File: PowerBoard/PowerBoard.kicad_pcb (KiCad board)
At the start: 2 copper layers, 95 x 72 mm, 26 parts, among them J1 AC_IN, J2 RelayCoil, J3 GATE_DRIVE, J4 LOGIC, J5 DC_LINK, K1 ALQ305

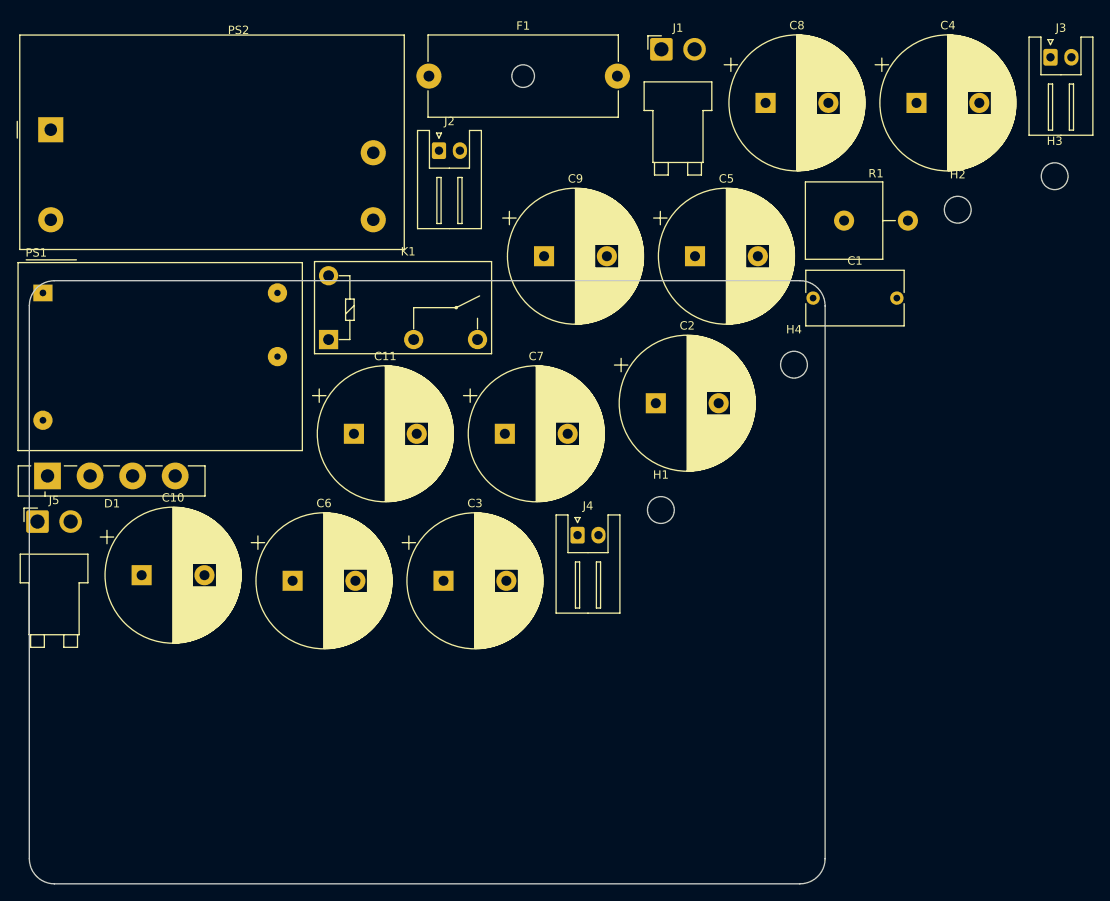
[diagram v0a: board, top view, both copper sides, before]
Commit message: コンデンサを一つ減らして配線完了
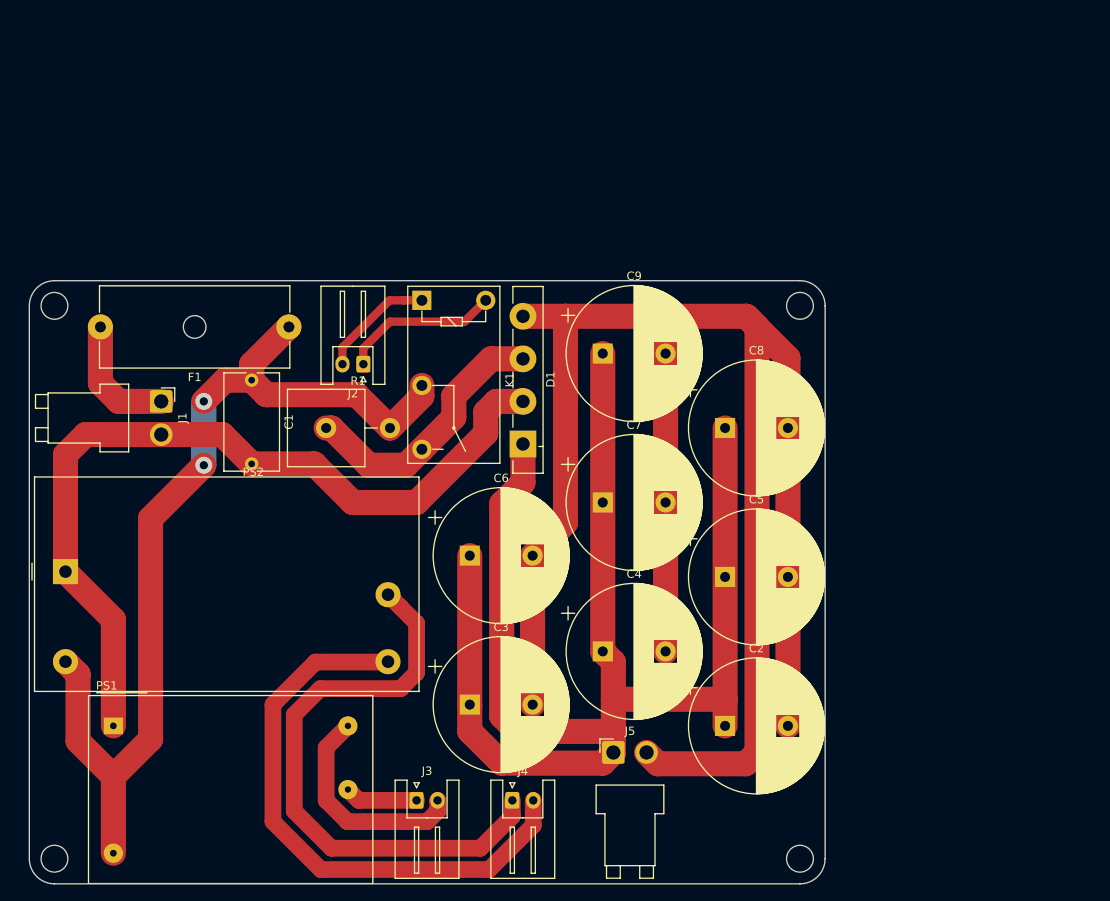
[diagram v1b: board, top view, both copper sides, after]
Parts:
- removed C10, C11: 150u, Capacitor_THT:CP_Radial_D16.0mm_P7.50mm
- moved J3 116.6 mm to (-1.27, 26.0)
- moved H4 106.2 mm to (-44.5, 33.0)
- moved H3 87.0 mm to (44.5, 33.0)
- moved H1 76.4 mm to (-44.5, -33.0)
- moved C4 75.4 mm to (21.0, 8.26)
- moved J5 74.1 mm to (22.2, 20.3)
- moved J1 73.0 mm to (-31.8, -21.6), turned to 270 degrees
- moved C1 67.7 mm to (-21.0, -24.1), turned to 270 degrees
- moved R1 66.6 mm to (-12.1, -18.4)
- moved D1 56.9 mm to (11.4, -16.5), turned to 90 degrees
- moved PS2 52.8 mm to (-43.2, -1.27)
- moved PS1 52.4 mm to (-37.5, 17.1)
- moved C2 39.4 mm to (35.6, 17.1)
- moved C8 39.1 mm to (35.6, -18.4)
- moved C5 38.5 mm to (35.6, -0.64)
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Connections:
- D1 pad 2: Net-(D1-Pad2) -> Net-(C1-Pad2)
- D1 pad 3: Net-(C1-Pad2) -> Net-(D1-Pad3)
- K1 pad 1: Net-(J2-Pad1) -> Net-(J2-Pad2)
- K1 pad 3: Net-(D1-Pad2) -> Net-(D1-Pad3)
- K1 pad 5: Net-(J2-Pad2) -> Net-(J2-Pad1)
- R1 pad 1: Net-(D1-Pad2) -> Net-(D1-Pad3)
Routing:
- net Net-(C2-Pad2): track 0.00 -> 232.6 mm
- net Net-(C2-Pad1): track 0.00 -> 184.9 mm
- net Net-(C1-Pad1): track 0.00 -> 115.0 mm, vias 0 -> 2
- net Net-(C1-Pad2): track 0.00 -> 100.2 mm
- net Net-(J4-Pad1): track 0.00 -> 70.3 mm
- net Net-(J4-Pad2): track 0.00 -> 68.4 mm
- net Net-(D1-Pad3): track 0.00 -> 32.1 mm
- net Net-(J3-Pad2): track 0.00 -> 26.2 mm
- net Net-(J2-Pad1): track 0.00 -> 18.9 mm
- net Net-(F1-Pad2): track 0.00 -> 14.9 mm
- net Net-(J2-Pad2): track 0.00 -> 13.8 mm
- net Net-(J3-Pad1): track 0.00 -> 8.73 mm
